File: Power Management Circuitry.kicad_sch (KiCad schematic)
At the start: 26 parts, among them J1 Barrel_Jack_Switch, Q1 AO3401A, Q2 SI2302, SW2 SW_DPDT_x2, U2 AMS1117-3.3, U3 AMS1117-5.0, U4 LM324, U5 LM339

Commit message: Rev 3.2
Cleaned Up Schematic
Revised Layout
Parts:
- added R11: 0 Ω, Resistor_SMD:R_1206_3216Metric_Pad1.30x1.75mm_HandSolder, symbol Device:R
- R7, R8: value 1 Ω -> 0.22 Ω
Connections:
- net +3V3: now also R10.2; no longer R10.1
- net +5V: now also RV1.1, R11.1; no longer RV1.3
- net at R10.2: now also R10.1; no longer R10.2
- net at U4.3 (+), U4.7: now also RV1.3; no longer RV1.1
- net V_{In} (Unfused): now reaches J1.1, R4.2, SW2.6 (C), U5.9 (+)
- new net +5V_NetTie: R11.2
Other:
- note added: "7 - 12 V Barrel Jack"
- note added: "Over Current Protection"
- note added: "Power Flags"
- note added: "Power Regulators"
- note added: "Power Source Switcher"
- note added: "To Do: ~Priority Switch to select which 5V source is the dominant~ DONE"
- note added: "USB Power LED Indicator"
- note added: "~Two Seperate Op-Amps needed due to difference in power source requirements (Rail selector won't work if the op amp is powered from the +12V)~ DONE"
- note removed: "To Do: ~Priority Switch to select which 5V source is the dominant~"
- note removed: "Two Seperate Op-Amps needed due to difference in power source requirements (Rail selector won't work if the op amp is powered from the +12V)"
- moved on the sheet: C5, C6, C7, C8, D1, F1, J1, Q1, Q2, R10, R3, R4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

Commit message: Schematic Organization
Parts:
- added J8, J9: Conn_01x04_Socket, Connector_PinSocket_2.54mm:PinSocket_1x04_P2.54mm_Vertical, symbol Connector:Conn_01x04_Socket
- Q2: footprint Package_TO_SOT_SMD:SOT-23_Handsoldering -> Package_TO_SOT_SMD:SOT-23
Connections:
- net +3V3: now also J9.1 (Pin_1), J9.2 (Pin_2)
- net +5V_{OCP}: now also J8.1 (Pin_1), J8.2 (Pin_2)
- net GND: now also J8.3 (Pin_3), J8.4 (Pin_4), J9.3 (Pin_3), J9.4 (Pin_4)
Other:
- note added: "Power Pins"
- moved on the sheet: R11

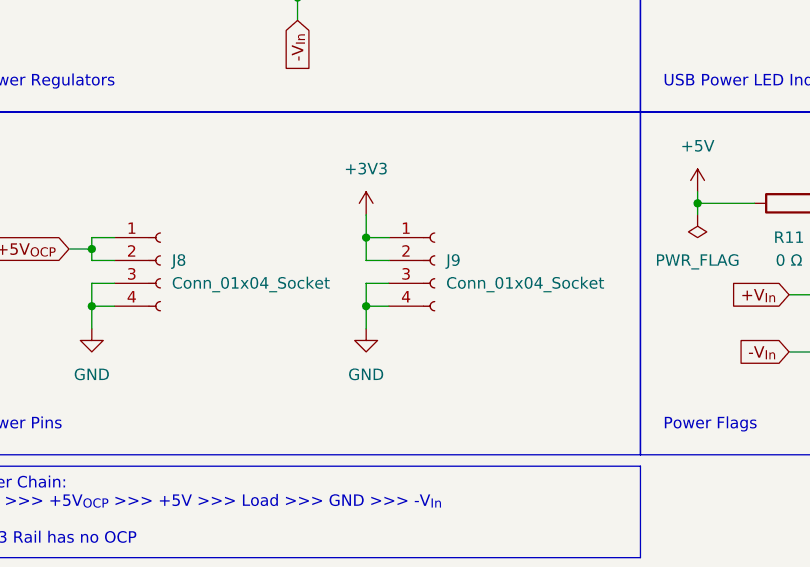
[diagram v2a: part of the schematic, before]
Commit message: Added I2C Labels
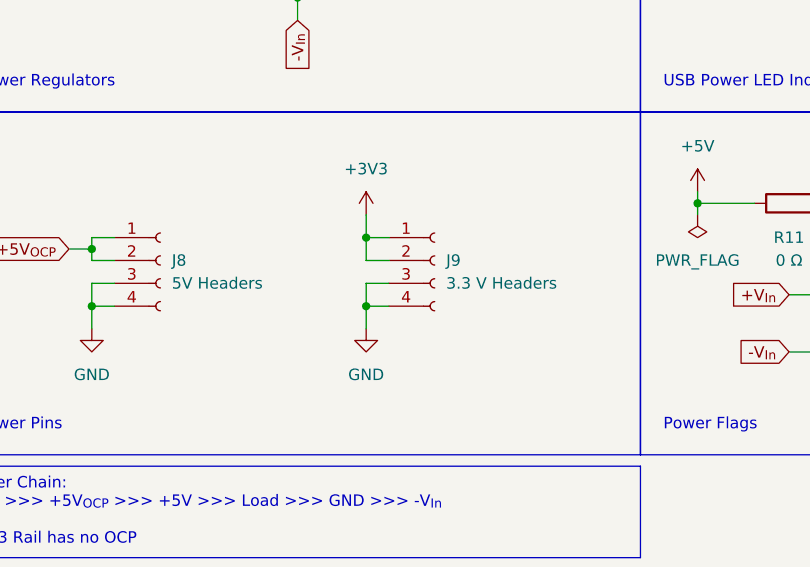
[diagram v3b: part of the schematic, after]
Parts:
- J8: value Conn_01x04_Socket -> 5V Headers
- J9: value Conn_01x04_Socket -> 3.3 V Headers
- Q2: footprint Package_TO_SOT_SMD:SOT-23 -> Package_TO_SOT_SMD:SOT-23_Handsoldering
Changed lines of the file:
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@@
       (effects (font (size 1.27 1.27)) (justify left))
     )
-    (property "Value" "Conn_01x04_Socket" (at 67.31 120.65 0)
+    (property "Value" "3.3 V Headers" (at 67.31 120.65 0)
       (effects (font (size 1.27 1.27)) (justify left))
     )
@@
       (effects (font (size 1.27 1.27)) (justify left))
     )
-    (property "Value" "Conn_01x04_Socket" (at 36.83 120.65 0)
+    (property "Value" "5V Headers" (at 36.83 120.65 0)
       (effects (font (size 1.27 1.27)) (justify left))
     )
@@
       (effects (font (size 1.27 1.27)))
     )
-    (property "Footprint" "Package_TO_SOT_SMD:SOT-23" (at 245.745 53.34 0)
+    (property "Footprint" "Package_TO_SOT_SMD:SOT-23_Handsoldering" (at 245.745 53.34 0)
       (effects (font (size 1.27 1.27) italic) (justify left) hide)
     )

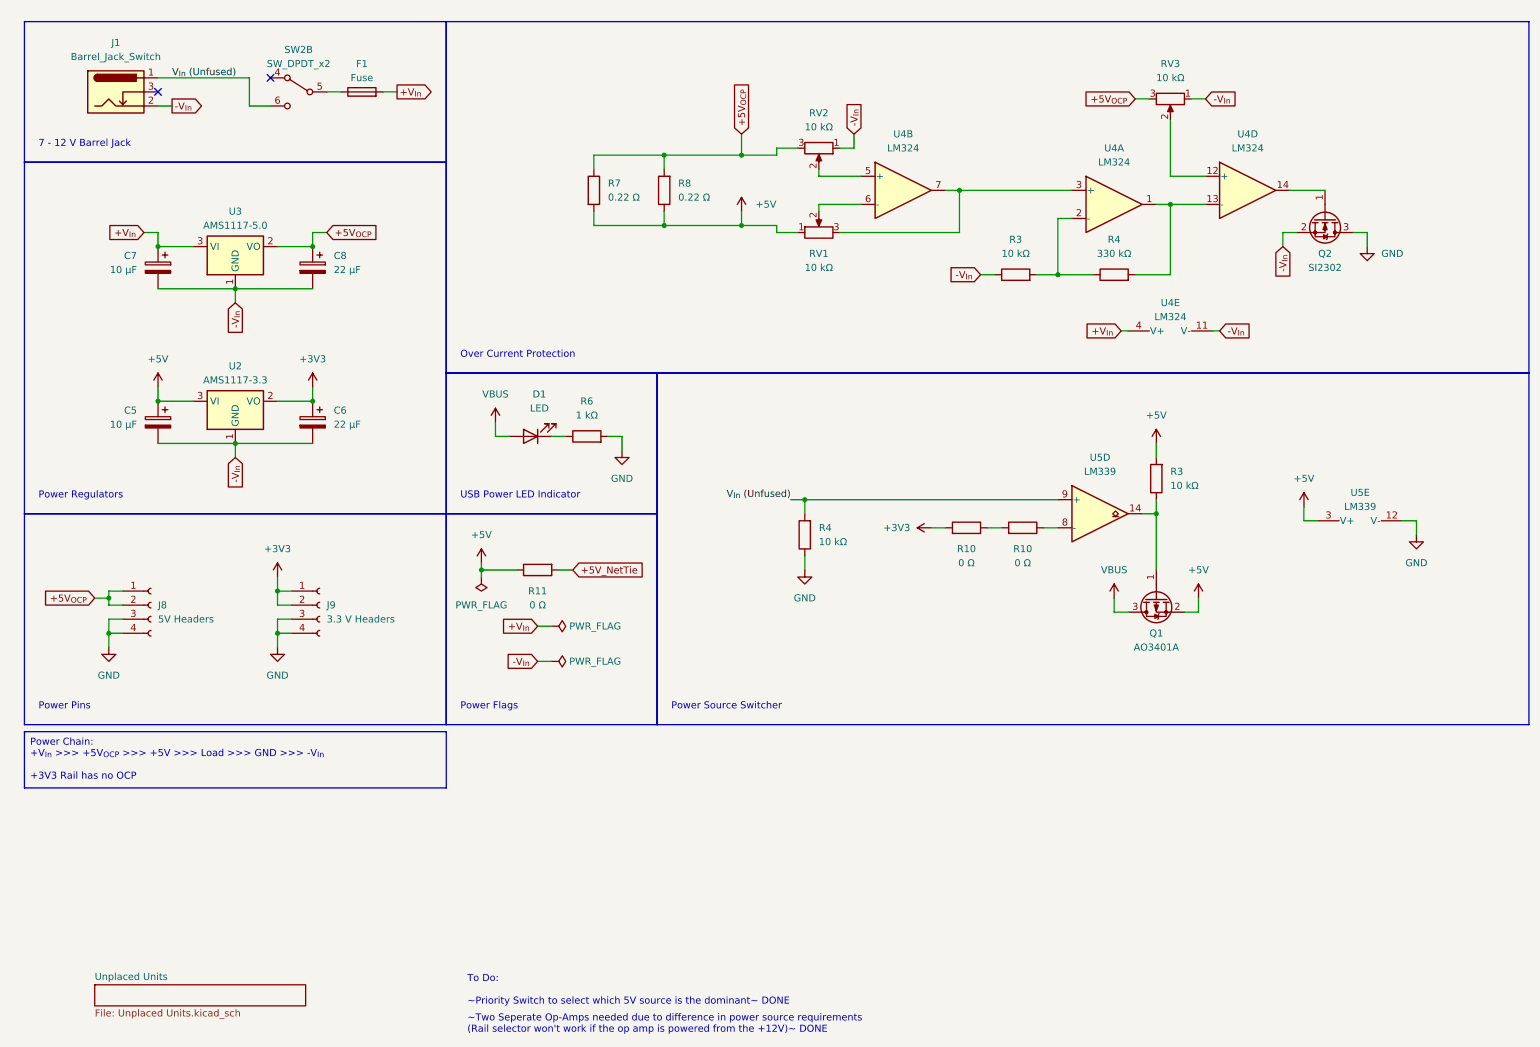
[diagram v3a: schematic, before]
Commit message: Improved Schematics' Readability
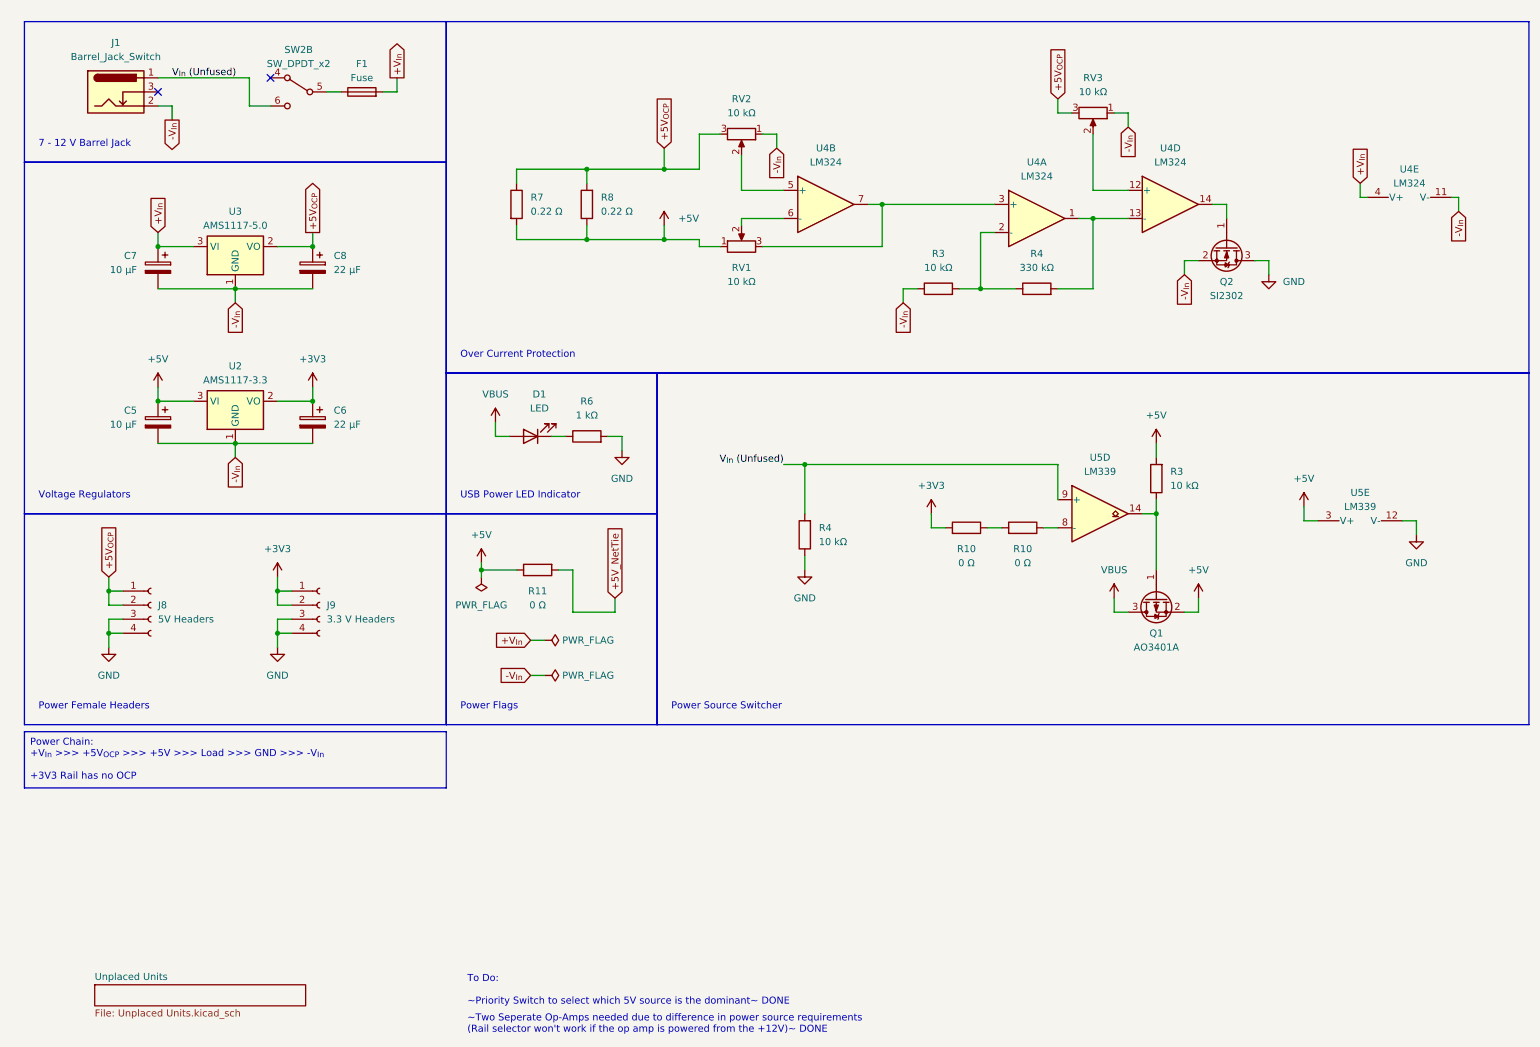
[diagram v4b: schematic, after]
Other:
- note added: "Power Female Headers"
- note added: "Voltage Regulators"
- note removed: "Power Pins"
- note removed: "Power Regulators"
- moved on the sheet: Q2, R3, R4, R7, R8, RV1, RV2, RV3, U4A, U4B, U4D, U4E

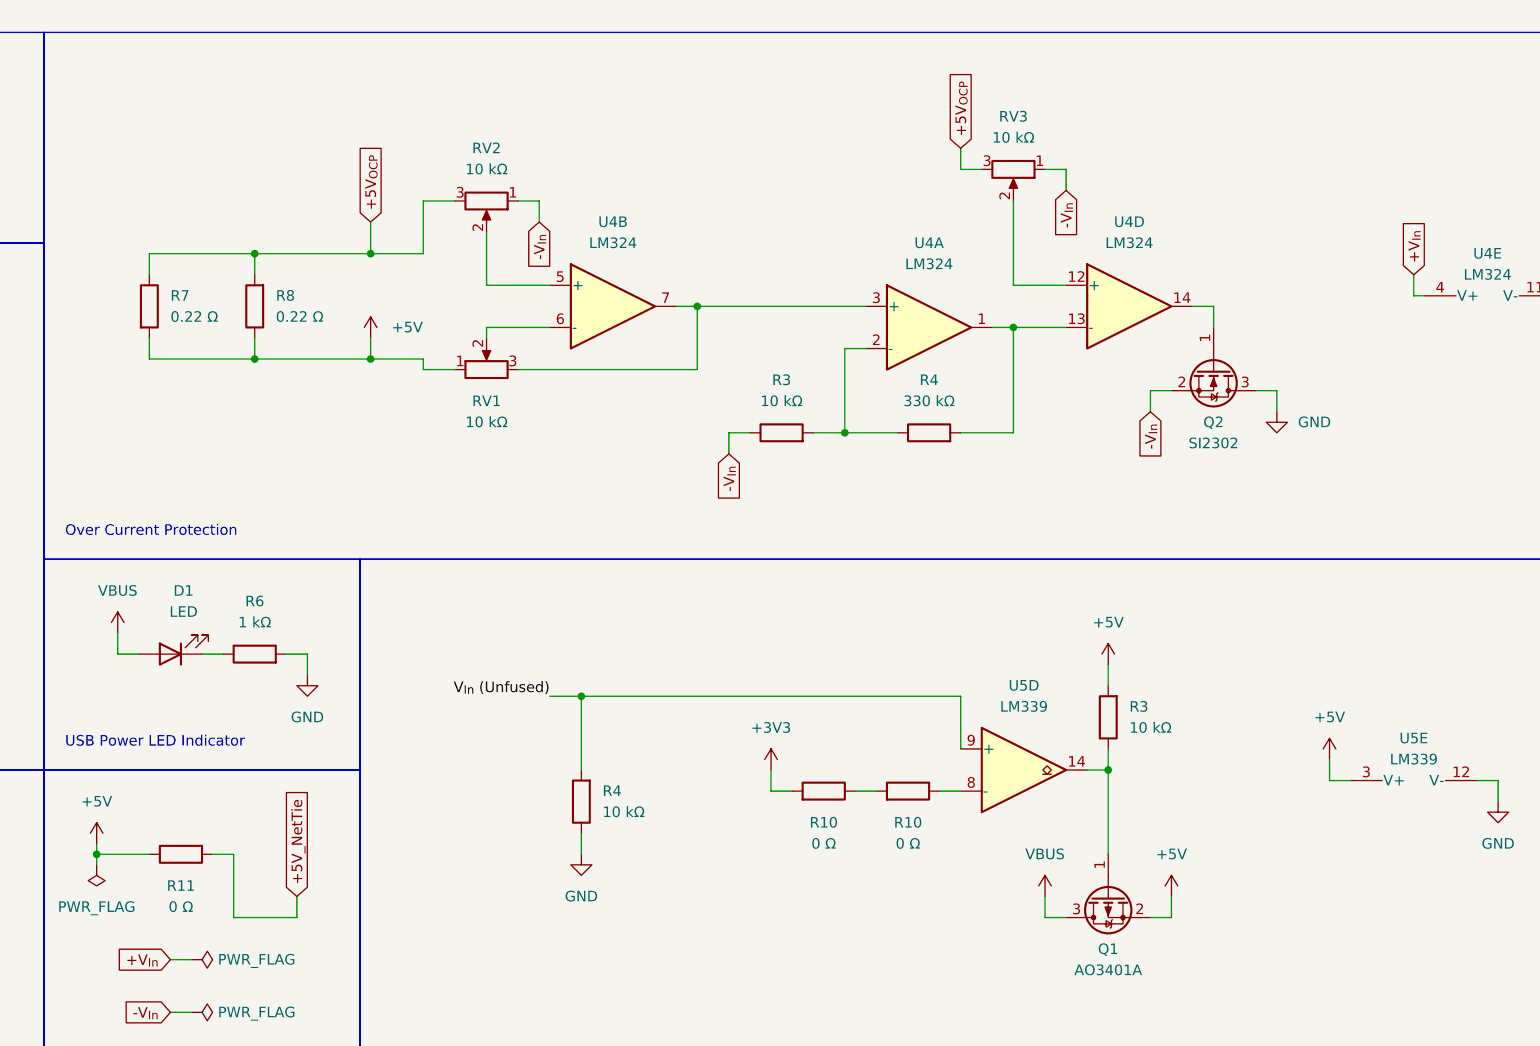
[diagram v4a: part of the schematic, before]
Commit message: More Touch Ups
Tidied the schematic
Added Dimensions of the PCB on User.Drawings Layer
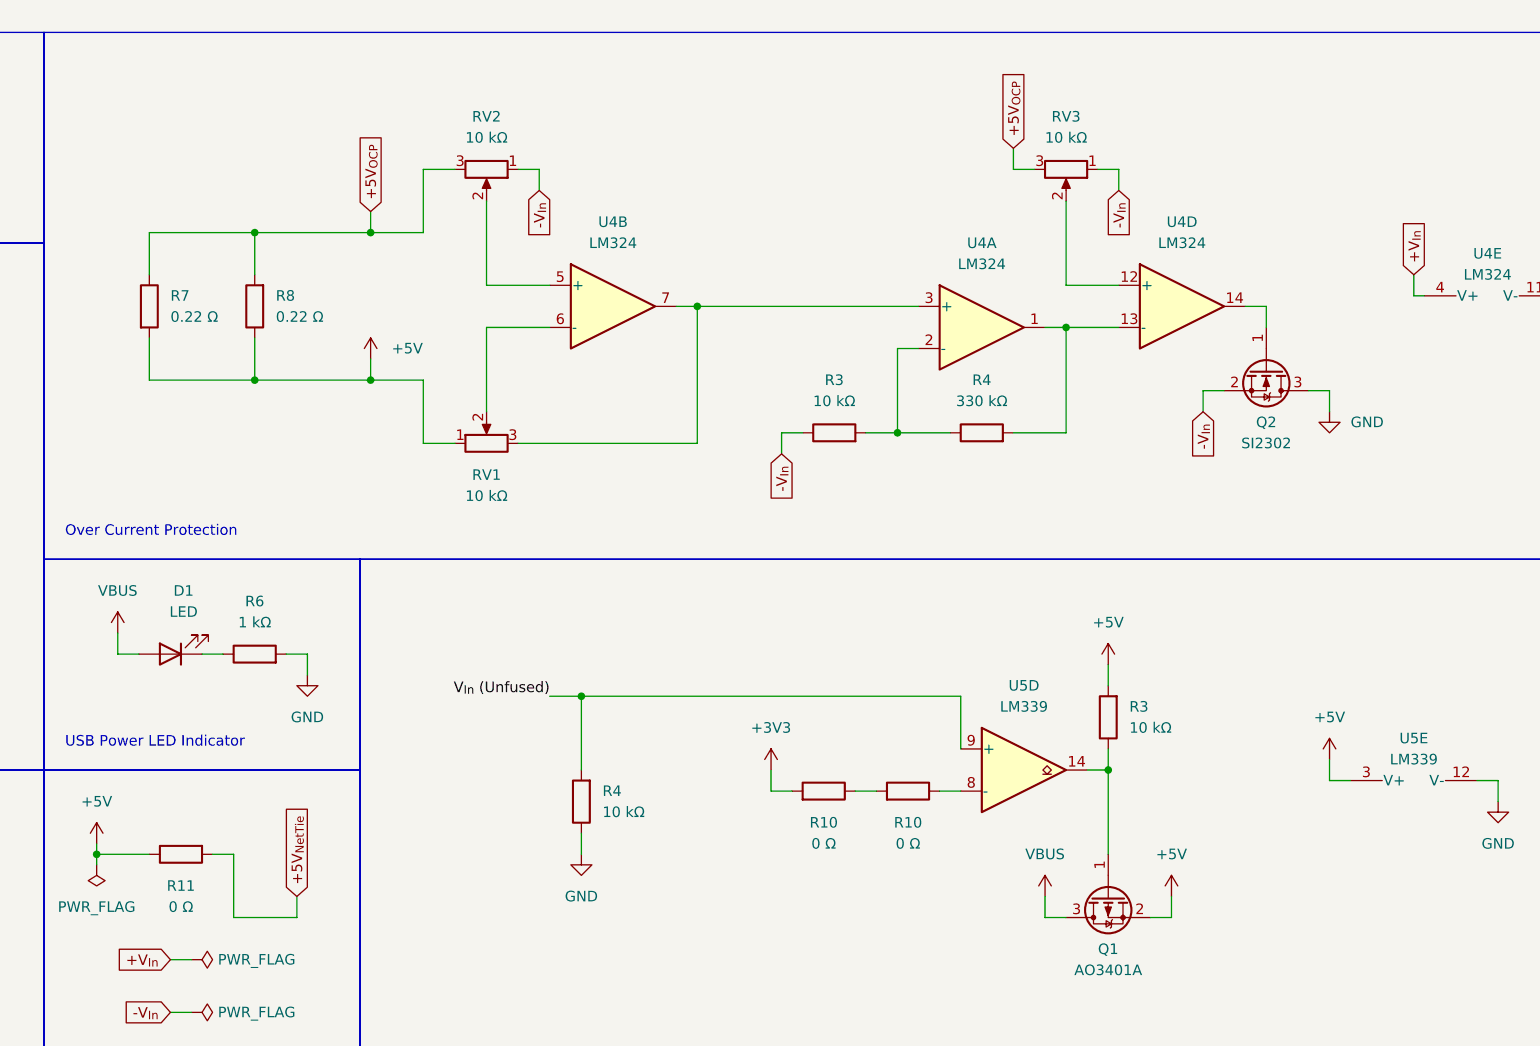
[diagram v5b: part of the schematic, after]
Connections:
- net +5V_NetTie renamed +5V_{NetTie}
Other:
- moved on the sheet: Q2, R3, R4, RV1, RV2, RV3, U4A, U4D

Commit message: New Subrevision
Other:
- note added: "http://store.logicneed.com/product/20510"
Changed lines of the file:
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@@
     (stroke (width 0) (type default))
   )
-  (wire (pts (xy 199.39 92.71) (xy 199.39 99.06))
+  (wire (pts (xy 196.85 92.71) (xy 196.85 99.06))
     (stroke (width 0) (type default))
   )
@@
     (stroke (width 0) (type default))
   )
+  (wire (pts (xy 196.85 99.06) (xy 199.39 99.06))
+    (stroke (width 0) (type default))
+  )
   (wire (pts (xy 134.62 62.23) (xy 134.62 54.61))
     (stroke (width 0) (type default))
@@
     (stroke (width 0) (type default))
   )
-  (wire (pts (xy 153.67 92.71) (xy 199.39 92.71))
+  (wire (pts (xy 153.67 92.71) (xy 196.85 92.71))
     (stroke (width 0) (type default))
   )
@@
     (effects (font (size 1.27 1.27)) (justify left bottom))
   )
+  (text "http://store.logicneed.com/product/20510" (at 158.75 161.29 0)
+    (effects (font (size 1.27 1.27)) (justify left bottom))
+  )
